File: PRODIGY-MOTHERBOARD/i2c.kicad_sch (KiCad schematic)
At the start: 7 parts, among them U13 PCA9306DC, U14 SN74LVC1T45DBV

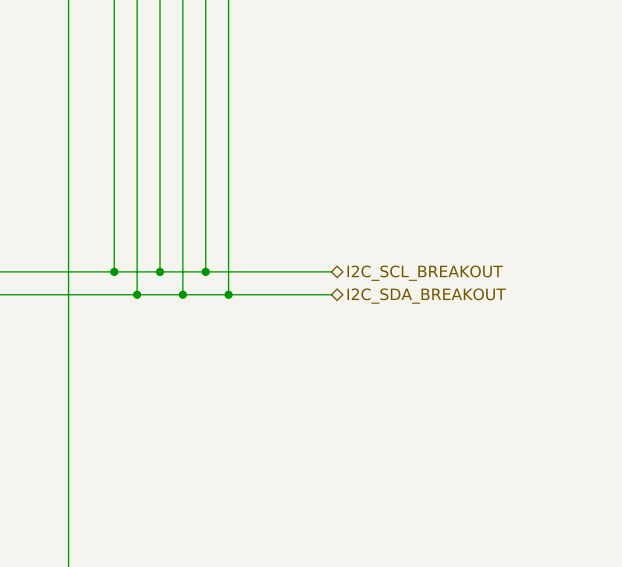
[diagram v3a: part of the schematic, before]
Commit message: Analog schematic finished, except the joystick part.
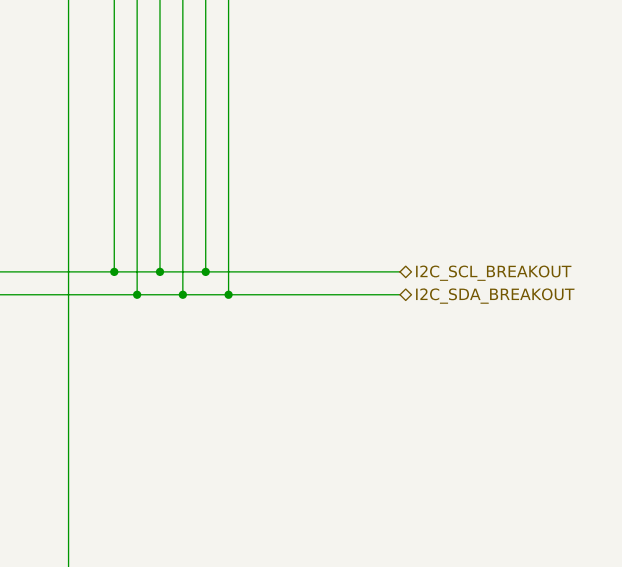
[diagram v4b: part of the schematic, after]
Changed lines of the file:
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@@
+	(wire
+		(pts
+			(xy 218.44 109.22) (xy 237.49 109.22)
+		)
+		(stroke
+			(width 0)
+			(type default)
+		)
+	)
 	(wire
 		(pts
@@
 	(wire
 		(pts
-			(xy 218.44 109.22) (xy 229.87 109.22)
-		)
-		(stroke
-			(width 0)
-			(type default)
-		)
-	)
-	(wire
-		(pts
 			(xy 77.47 106.68) (xy 102.87 106.68)
 		)
@@
 	(wire
 		(pts
+			(xy 215.9 106.68) (xy 237.49 106.68)
+		)
+		(stroke
+			(width 0)
+			(type default)
+		)
+	)
+	(wire
+		(pts
 			(xy 200.66 63.5) (xy 200.66 149.86)
 		)
@@
 		(pts
 			(xy 120.65 162.56) (xy 130.81 162.56)
-		)
-		(stroke
-			(width 0)
-			(type default)
-		)
-	)
-	(wire
-		(pts
-			(xy 215.9 106.68) (xy 229.87 106.68)
 		)
 		(stroke
@@
 	(hierarchical_label "I2C_SCL_BREAKOUT"
 		(shape bidirectional)
-		(at 229.87 106.68 0)
+		(at 237.49 106.68 0)
 		(fields_autoplaced yes)
 		(effects
@@
 	(hierarchical_label "I2C_SDA_BREAKOUT"
 		(shape bidirectional)
-		(at 229.87 109.22 0)
+		(at 237.49 109.22 0)
 		(fields_autoplaced yes)
 		(effects

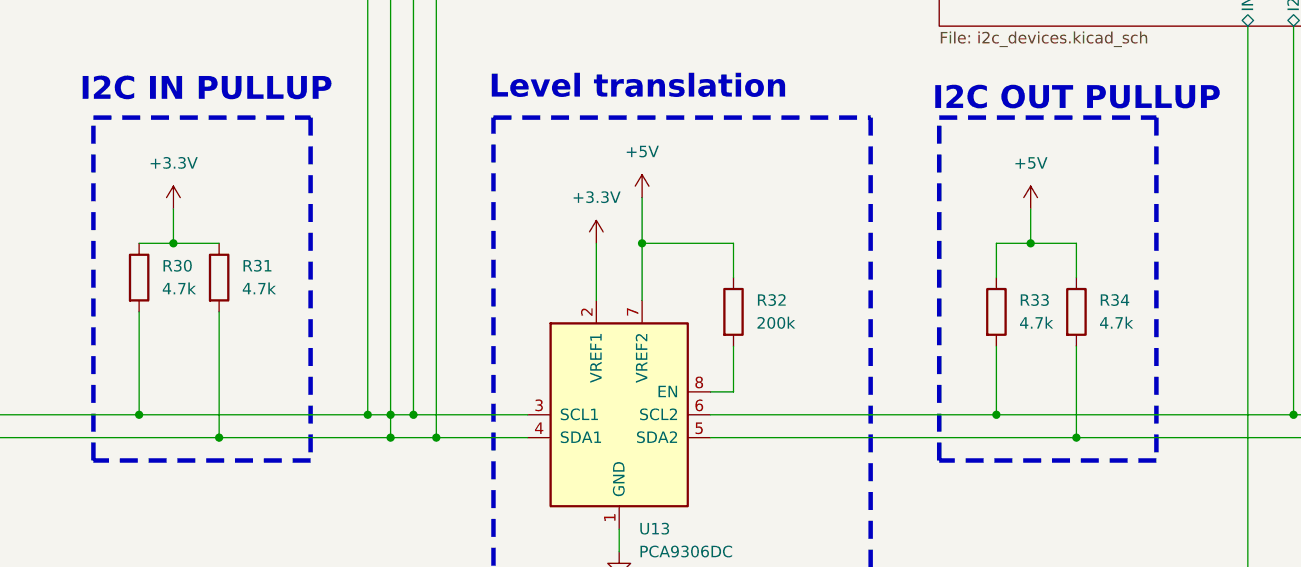
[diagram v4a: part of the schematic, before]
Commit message: Added proper debounce filter elements to buttons.
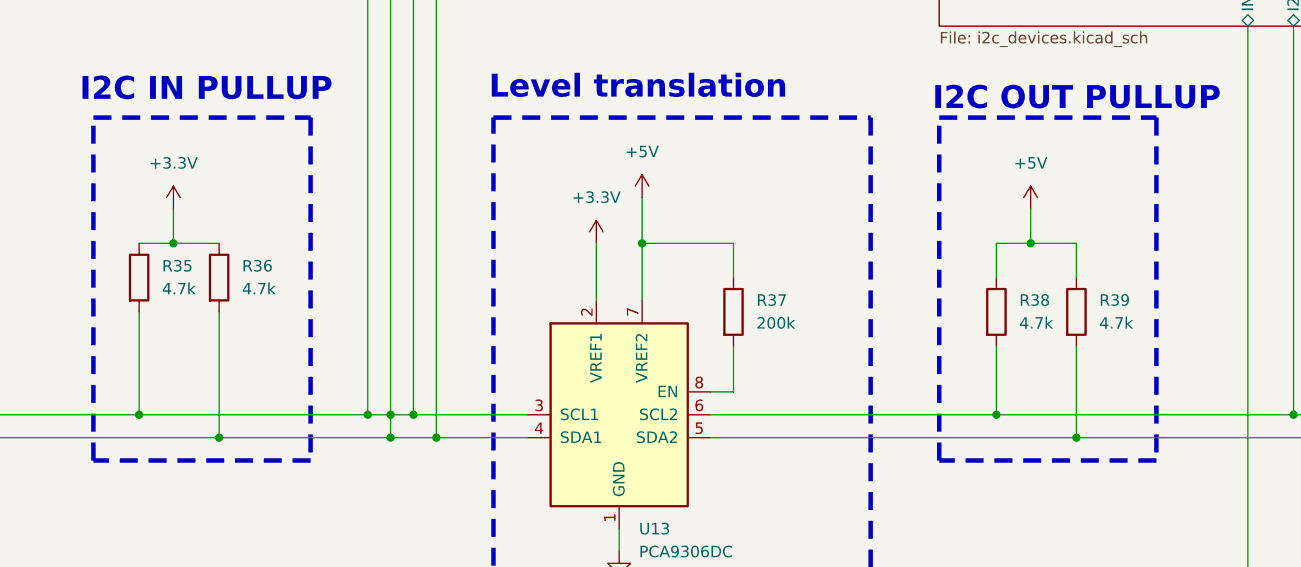
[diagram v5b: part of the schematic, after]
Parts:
- renumbered R30 to R35, R31 to R36, R32 to R37, R33 to R38, R34 to R39
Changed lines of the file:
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@@
 		(dnp no)
 		(fields_autoplaced yes)
-		(property "Reference" "R34"
+		(property "Reference" "R39"
 			(at 184.15 93.9799 0)
 			(effects
@@
 			(project "PRODIGY-MOTHERBOARD"
 				(path "/f1c25860-8989-4190-bd24-2491d23ca7d9/68745e9f-546d-4e12-ac2b-ba23aeab0093"
-					(reference "R34")
+					(reference "R39")
 					(unit 1)
 				)
@@
 		(dnp no)
 		(fields_autoplaced yes)
-		(property "Reference" "#PWR076"
+		(property "Reference" "#PWR081"
 			(at 133.35 86.36 0)
 			(effects
@@
 			(project "PRODIGY-MOTHERBOARD"
 				(path "/f1c25860-8989-4190-bd24-2491d23ca7d9/68745e9f-546d-4e12-ac2b-ba23aeab0093"
-					(reference "#PWR076")
+					(reference "#PWR081")
 					(unit 1)
 				)
@@
 		(dnp no)
 		(fields_autoplaced yes)
-		(property "Reference" "R31"
+		(property "Reference" "R36"
 			(at 88.9 90.1699 0)
 			(effects
@@
 			(project "PRODIGY-MOTHERBOARD"
 				(path "/f1c25860-8989-4190-bd24-2491d23ca7d9/68745e9f-546d-4e12-ac2b-ba23aeab0093"
-					(reference "R31")
+					(reference "R36")
 					(unit 1)
 				)
@@
 		(dnp no)
 		(fields_autoplaced yes)
-		(property "Reference" "#PWR072"
+		(property "Reference" "#PWR084"
 			(at 128.27 91.44 0)
 			(effects
@@
 			(project "PRODIGY-MOTHERBOARD"
 				(path "/f1c25860-8989-4190-bd24-2491d23ca7d9/68745e9f-546d-4e12-ac2b-ba23aeab0093"
-					(reference "#PWR072")
+					(reference "#PWR084")
 					(unit 1)
 				)
@@
 		(dnp no)
 		(fields_autoplaced yes)
-		(property "Reference" "#PWR078"
+		(property "Reference" "#PWR083"
 			(at 176.53 87.63 0)
 			(effects
@@
 			(project "PRODIGY-MOTHERBOARD"
 				(path "/f1c25860-8989-4190-bd24-2491d23ca7d9/68745e9f-546d-4e12-ac2b-ba23aeab0093"
-					(reference "#PWR078")
+					(reference "#PWR083")
 					(unit 1)
 				)
@@
 		(dnp no)
 		(fields_autoplaced yes)
-		(property "Reference" "#PWR071"
+		(property "Reference" "#PWR082"
 			(at 81.28 87.63 0)
 			(effects
@@
 			(project "PRODIGY-MOTHERBOARD"
 				(path "/f1c25860-8989-4190-bd24-2491d23ca7d9/68745e9f-546d-4e12-ac2b-ba23aeab0093"
-					(reference "#PWR071")
+					(reference "#PWR082")
 					(unit 1)
 				)
@@
 		(on_board yes)
 		(dnp no)
-		(property "Reference" "#PWR074"
+		(property "Reference" "#PWR085"
 			(at 130.81 128.27 0)
 			(effects
@@
 			(project "PRODIGY-MOTHERBOARD"
 				(path "/f1c25860-8989-4190-bd24-2491d23ca7d9/68745e9f-546d-4e12-ac2b-ba23aeab0093"
-					(reference "#PWR074")
+					(reference "#PWR085")
 					(unit 1)
 				)
@@
 		(dnp no)
 		(fields_autoplaced yes)
-		(property "Reference" "#PWR075"
+		(property "Reference" "#PWR088"
 			(at 130.81 171.45 0)
 			(effects
@@
 			(project "PRODIGY-MOTHERBOARD"
 				(path "/f1c25860-8989-4190-bd24-2491d23ca7d9/68745e9f-546d-4e12-ac2b-ba23aeab0093"
-					(reference "#PWR075")
+					(reference "#PWR088")
 					(unit 1)
 				)
@@
 		(dnp no)
 		(fields_autoplaced yes)
-		(property "Reference" "R33"
+		(property "Reference" "R38"
 			(at 175.26 93.9799 0)
 			(effects
@@
 			(project "PRODIGY-MOTHERBOARD"
 				(path "/f1c25860-8989-4190-bd24-2491d23ca7d9/68745e9f-546d-4e12-ac2b-ba23aeab0093"
-					(reference "R33")
+					(reference "R38")
 					(unit 1)
 				)
@@
 		(dnp no)
 		(fields_autoplaced yes)
-		(property "Reference" "#PWR077"
+		(property "Reference" "#PWR086"
 			(at 133.35 139.7 0)
 			(effects
@@
 			(project "PRODIGY-MOTHERBOARD"
 				(path "/f1c25860-8989-4190-bd24-2491d23ca7d9/68745e9f-546d-4e12-ac2b-ba23aeab0093"
-					(reference "#PWR077")
+					(reference "#PWR086")
 					(unit 1)
 				)
@@
 		(dnp no)
 		(fields_autoplaced yes)
-		(property "Reference" "#PWR073"
+		(property "Reference" "#PWR087"
 			(at 128.27 143.51 0)
 			(effects
@@
 			(project "PRODIGY-MOTHERBOARD"
 				(path "/f1c25860-8989-4190-bd24-2491d23ca7d9/68745e9f-546d-4e12-ac2b-ba23aeab0093"
-					(reference "#PWR073")
+					(reference "#PWR087")
 					(unit 1)
 				)
@@
 		(dnp no)
 		(fields_autoplaced yes)
-		(property "Reference" "R32"
+		(property "Reference" "R37"
 			(at 146.05 93.9799 0)
 			(effects
@@
 			(project "PRODIGY-MOTHERBOARD"
 				(path "/f1c25860-8989-4190-bd24-2491d23ca7d9/68745e9f-546d-4e12-ac2b-ba23aeab0093"
-					(reference "R32")
+					(reference "R37")
 					(unit 1)
 				)
@@
 		(dnp no)
 		(fields_autoplaced yes)
-		(property "Reference" "R30"
+		(property "Reference" "R35"
 			(at 80.01 90.1699 0)
 			(effects
@@
 			(project "PRODIGY-MOTHERBOARD"
 				(path "/f1c25860-8989-4190-bd24-2491d23ca7d9/68745e9f-546d-4e12-ac2b-ba23aeab0093"
-					(reference "R30")
-					(unit 1)
-				)
+					(reference "R35")
+					(unit 1)
+				)
